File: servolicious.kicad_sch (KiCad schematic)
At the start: 14 parts, among them J1 Conn_01x03_Pin, J10 Barrel_Jack_MountingPin, J2 Conn_01x03_Pin, J3 Conn_01x03_Pin, J4 Conn_01x03_Pin, J5 Conn_01x03_Pin, J6 Conn_01x03_Pin, J7 Conn_01x03_Pin, J8 Conn_01x03_Pin, J9 Conn_01x03_Pin, U2 74HC164

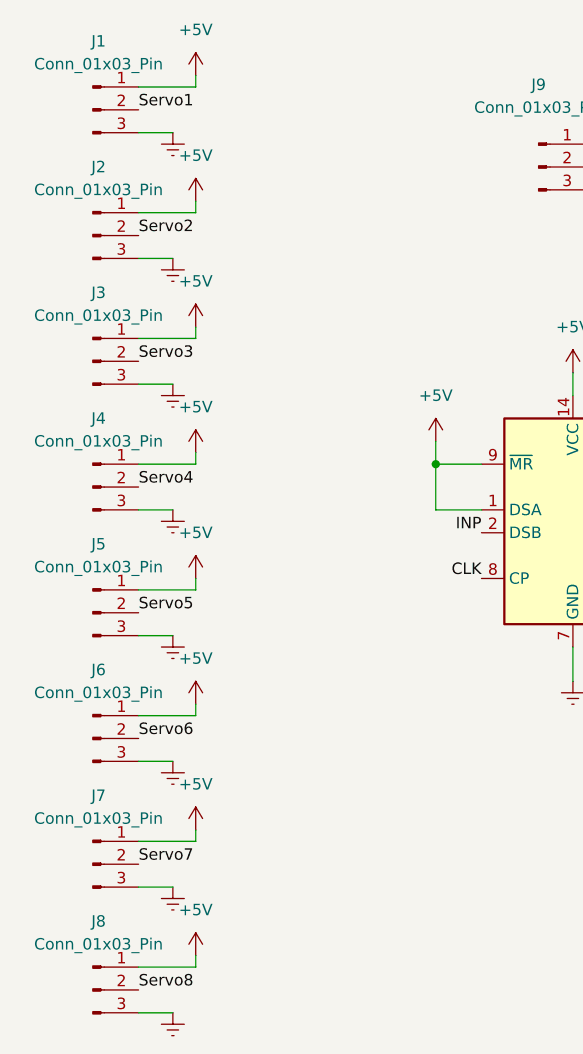
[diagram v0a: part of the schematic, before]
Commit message: Servo headers were wrong
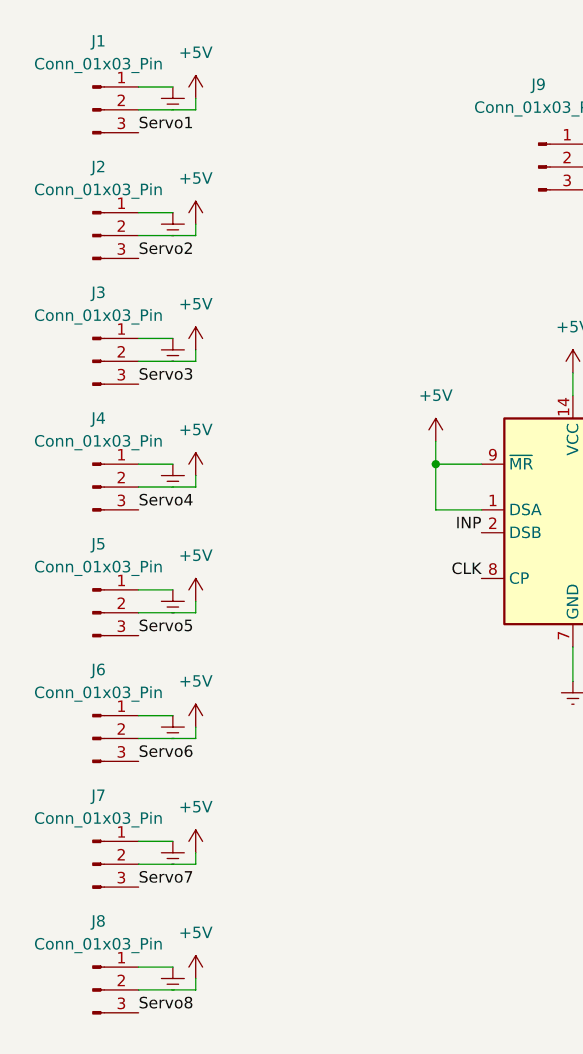
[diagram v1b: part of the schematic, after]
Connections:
- net +5V: now also J1.2 (Pin_2), J2.2 (Pin_2), J3.2 (Pin_2), J4.2 (Pin_2), J5.2 (Pin_2), J6.2 (Pin_2), J7.2 (Pin_2), J8.2 (Pin_2); no longer J1.1 (Pin_1), J2.1 (Pin_1), J3.1 (Pin_1), J4.1 (Pin_1), J5.1 (Pin_1), J6.1 (Pin_1), J7.1 (Pin_1), J8.1 (Pin_1)
- net Earth: now also J1.1 (Pin_1), J2.1 (Pin_1), J3.1 (Pin_1), J4.1 (Pin_1), J5.1 (Pin_1), J6.1 (Pin_1), J7.1 (Pin_1), J8.1 (Pin_1); no longer J1.3 (Pin_3), J2.3 (Pin_3), J3.3 (Pin_3), J4.3 (Pin_3), J5.3 (Pin_3), J6.3 (Pin_3), J7.3 (Pin_3), J8.3 (Pin_3)
- net Servo1: now also J1.3 (Pin_3); no longer J1.2 (Pin_2)
- net Servo2: now also J2.3 (Pin_3); no longer J2.2 (Pin_2)
- net Servo3: now also J3.3 (Pin_3); no longer J3.2 (Pin_2)
- net Servo4: now also J4.3 (Pin_3); no longer J4.2 (Pin_2)
- net Servo5: now also J5.3 (Pin_3); no longer J5.2 (Pin_2)
- net Servo6: now also J6.3 (Pin_3); no longer J6.2 (Pin_2)
- net Servo7: now also J7.3 (Pin_3); no longer J7.2 (Pin_2)
- net Servo8: now also J8.3 (Pin_3); no longer J8.2 (Pin_2)

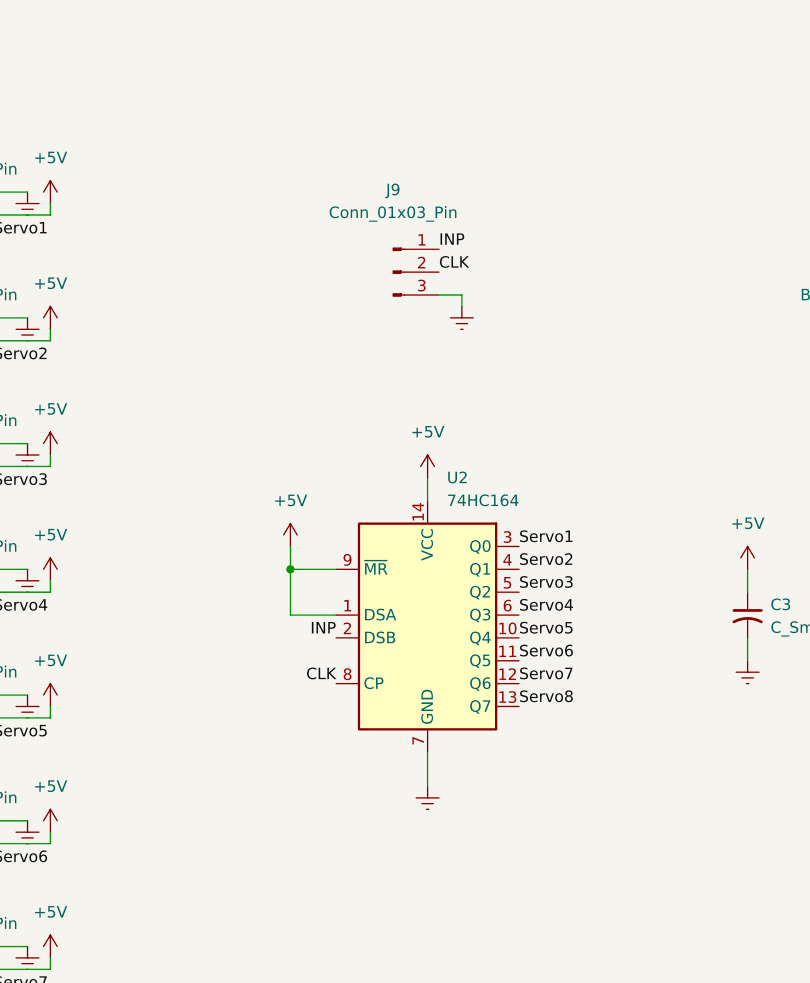
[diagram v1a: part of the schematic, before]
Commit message: Switch to latched shift register
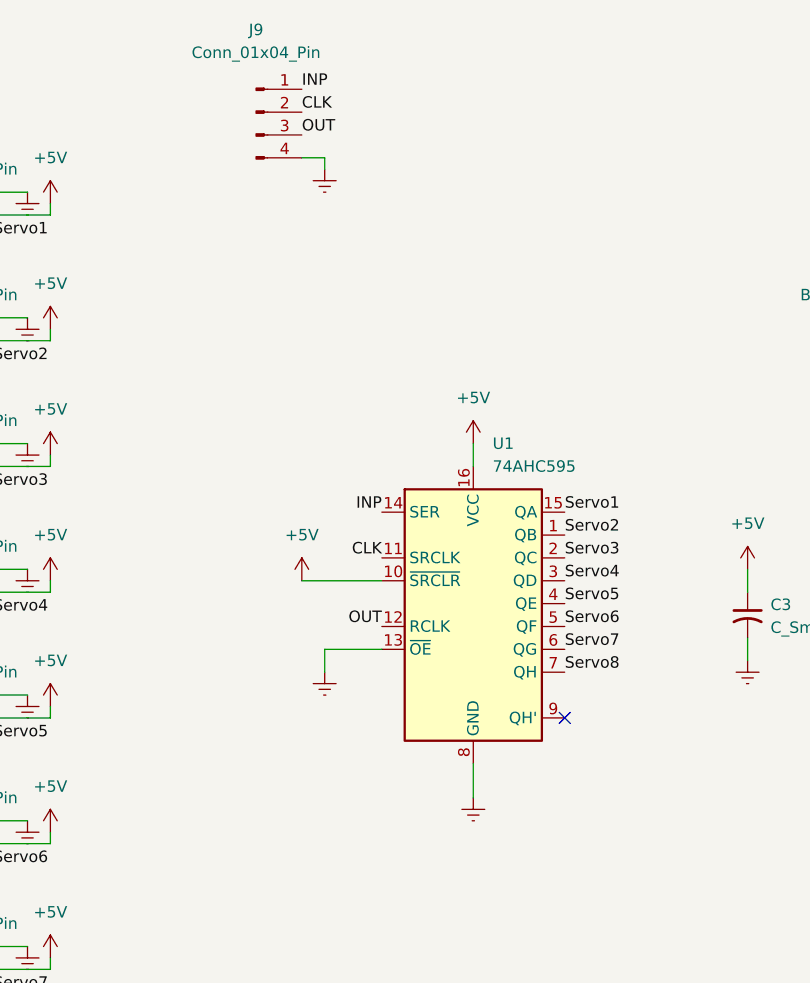
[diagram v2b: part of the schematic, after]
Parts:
- removed J9: Conn_01x03_Pin, Connector_PinHeader_2.54mm:PinHeader_1x03_P2.54mm_Vertical, symbol Connector:Conn_01x03_Pin
- removed U2: 74HC164, Package_SO:SOIC-14_3.9x8.7mm_P1.27mm, symbol 74xx:74HC164
- added J9: Conn_01x04_Pin, Connector_PinHeader_2.54mm:PinHeader_1x04_P2.54mm_Vertical, symbol Connector:Conn_01x04_Pin
- added U1: 74AHC595, Package_SO:SOIC-16W_5.3x10.2mm_P1.27mm, symbol 74xx:74AHC595
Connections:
- net +5V: now also U1.10 (~{SRCLR}), U1.16 (VCC)
- net CLK: now also J9.2 (Pin_2), U1.11 (SRCLK)
- net Earth: now also J9.4 (Pin_4), U1.13 (~{OE}), U1.8 (GND)
- net INP: now also J9.1 (Pin_1), U1.14 (SER)
- net Servo1: now also U1.15 (QA)
- net Servo2: now also U1.1 (QB)
- net Servo3: now also U1.2 (QC)
- net Servo4: now also U1.3 (QD)
- net Servo5: now also U1.4 (QE)
- net Servo6: now also U1.5 (QF)
- net Servo7: now also U1.6 (QG)
- net Servo8: now also U1.7 (QH)
- new net OUT: J9.3 (Pin_3), U1.12 (RCLK)
- no-connect marks 1 -> 2

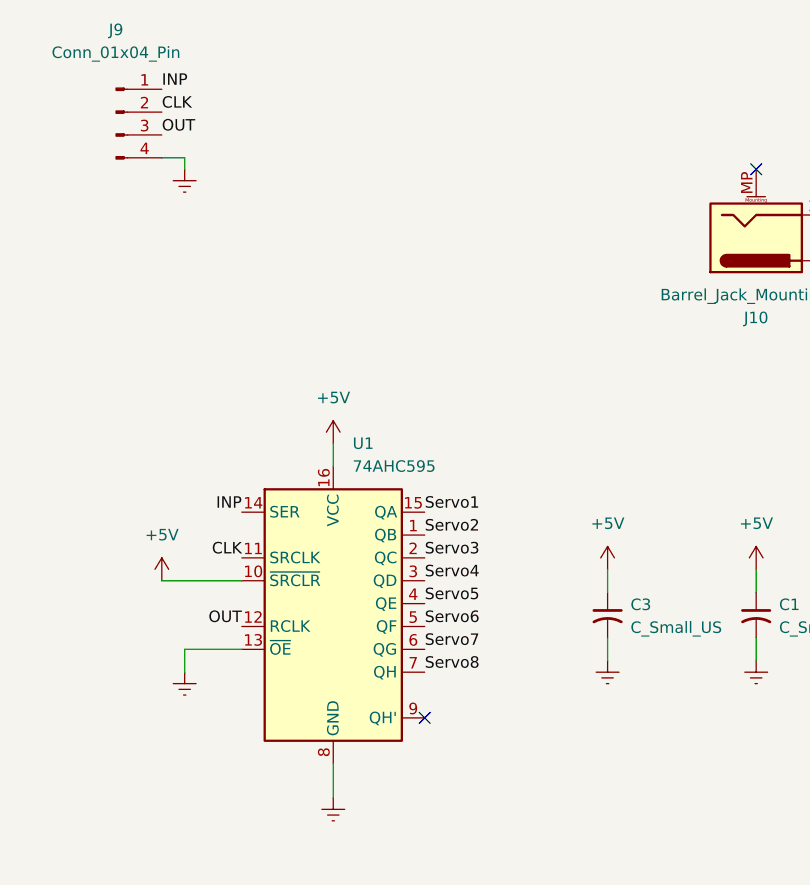
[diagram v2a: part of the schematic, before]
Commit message: Add daisy out
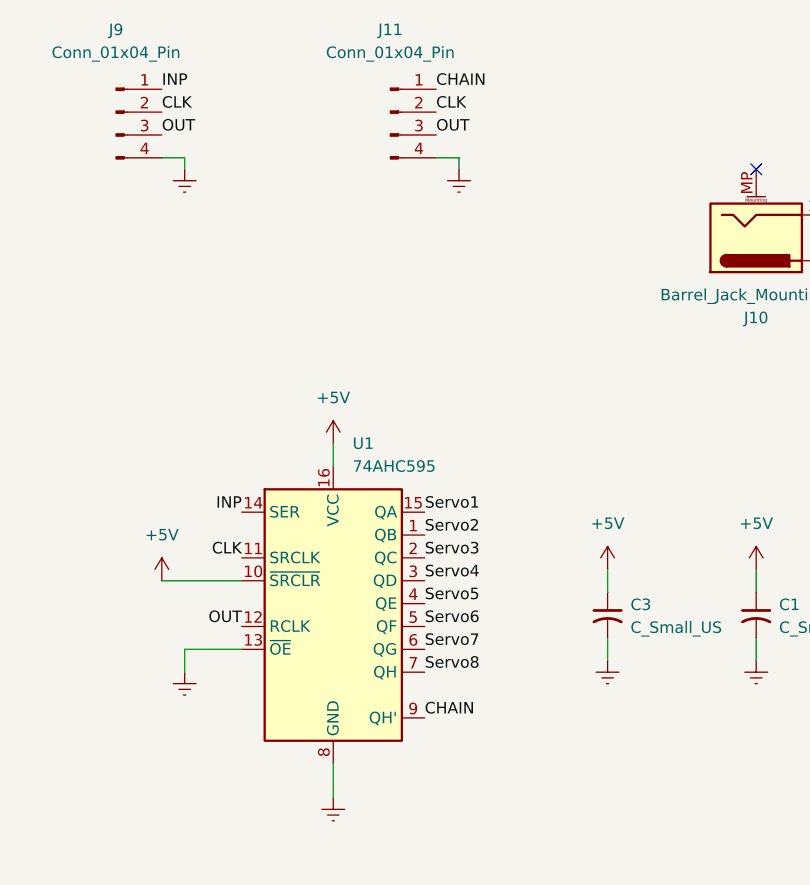
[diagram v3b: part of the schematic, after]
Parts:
- added J11: Conn_01x04_Pin, Connector_PinHeader_2.54mm:PinHeader_1x04_P2.54mm_Vertical, symbol Connector:Conn_01x04_Pin
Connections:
- net CLK: now also J11.2 (Pin_2)
- net Earth: now also J11.4 (Pin_4)
- net OUT: now also J11.3 (Pin_3)
- net CHAIN: now reaches U1.9 (QH')
- net CHAIN: now also J11.1 (Pin_1)
- no-connect marks 2 -> 1
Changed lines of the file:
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@@
 		(at 160.02 46.99)
 	)
-	(no_connect
-		(at 123.19 107.95)
-	)
 	(wire
 		(pts
@@
 	(wire
 		(pts
+			(xy 127 46.99) (xy 127 45.72)
+		)
+		(stroke
+			(width 0)
+			(type default)
+		)
+	)
+	(wire
+		(pts
 			(xy 66.04 66.04) (xy 66.04 64.77)
 		)
@@
 	(wire
 		(pts
+			(xy 127 45.72) (xy 124.46 45.72)
+		)
+		(stroke
+			(width 0)
+			(type default)
+		)
+	)
+	(wire
+		(pts
 			(xy 59.69 66.04) (xy 66.04 66.04)
 		)
@@
 			(width 0)
 			(type default)
+		)
+	)
+	(label "CHAIN"
+		(at 124.46 38.1 0)
+		(effects
+			(font
+				(size 1.27 1.27)
+			)
+			(justify left bottom)
 		)
 	)
@@
 		)
 	)
+	(label "CHAIN"
+		(at 123.19 107.95 0)
+		(effects
+			(font
+				(size 1.27 1.27)
+			)
+			(justify left bottom)
+		)
+	)
 	(label "Servo2"
 		(at 59.69 68.58 0)
@@
 		)
 	)
+	(label "CLK"
+		(at 124.46 40.64 0)
+		(effects
+			(font
+				(size 1.27 1.27)
+			)
+			(justify left bottom)
+		)
+	)
 	(label "OUT"
 		(at 102.87 97.79 180)
@@
 	(label "Servo1"
 		(at 59.69 54.61 0)
+		(effects
+			(font
+				(size 1.27 1.27)
+			)
+			(justify left bottom)
+		)
+	)
+	(label "OUT"
+		(at 124.46 43.18 0)
 		(effects
 			(font
@@
 	(symbol
 		(lib_id "power:Earth")
+		(at 127 46.99 0)
+		(unit 1)
+		(exclude_from_sim no)
+		(in_bom yes)
+		(on_board yes)
+		(dnp no)
+		(fields_autoplaced yes)
+		(property "Reference" "#PWR030"
+			(at 127 53.34 0)
+			(effects
+				(font
+					(size 1.27 1.27)
+				)
+				(hide yes)
+			)
+		)
+		(property "Value" "Earth"
+			(at 127 52.07 0)
+			(effects
+				(font
+					(size 1.27 1.27)
+				)
+				(hide yes)
+			)
+		)
+		(property "Footprint" ""
+			(at 127 46.99 0)
+			(effects
+				(font
+					(size 1.27 1.27)
+				)
+				(hide yes)
+			)
+		)
+		(property "Datasheet" "~"
+			(at 127 46.99 0)
+			(effects
+				(font
+					(size 1.27 1.27)
+				)
+				(hide yes)
+			)
+		)
+		(property "Description" "Power symbol creates a global label with name \"Earth\""
+			(at 127 46.99 0)
+			(effects
+				(font
+					(size 1.27 1.27)
+				)
+				(hide yes)
+			)
+		)
+		(pin "1"
+		)
+		(instances
+			(project "servolicious"
+				(path "/c3a088af-77fe-4a0a-8cb5-e069078caf1a"
+					(reference "#PWR030")
+					(unit 1)
+				)
+			)
+		)
+	)
+	(symbol
+		(lib_id "power:Earth")
 		(at 173.99 60.96 0)
 		(unit 1)
@@
 					(unit 1)
 				)
+			)
+		)
+	)
+	(symbol
+		(lib_id "Connector:Conn_01x04_Pin")
+		(at 119.38 40.64 0)
+		(unit 1)
+		(exclude_from_sim no)
+		(in_bom yes)
+		(on_board yes)
+		(dnp no)
+		(property "Reference" "J11"
+			(at 119.38 31.496 0)
+			(effects
+				(font
+					(size 1.27 1.27)
+				)
+			)
+		)
+		(property "Value" "Conn_01x04_Pin"
+			(at 119.38 34.036 0)
+			(effects
+				(font
+					(size 1.27 1.27)
+				)
+			)
+		)
+		(property "Footprint" "Connector_PinHeader_2.54mm:PinHeader_1x04_P2.54mm_Vertical"
+			(at 119.38 40.64 0)
+			(effects
+				(font
+					(size 1.27 1.27)
+				)
+				(hide yes)
+			)
+		)
+		(property "Datasheet" "~"
+			(at 119.38 40.64 0)
+			(effects
+				(font
+					(size 1.27 1.27)
+				)
+				(hide yes)
+			)
+		)
+		(property "Description" "Generic connector, single row, 01x04, script generated"
+			(at 119.38 40.64 0)
+			(effects
+				(font
+					(size 1.27 1.27)
+				)
+				(hide yes)
+			)
+		)
+		(pin "2"
+		)
+		(pin "4"
+		)
+		(pin "3"
+		)
+		(pin "1"
+		)
+		(instances
+			(project "servolicious"
+				(path "/c3a088af-77fe-4a0a-8cb5-e069078caf1a"
+					(reference "J11")
+					(unit 1)
+				)

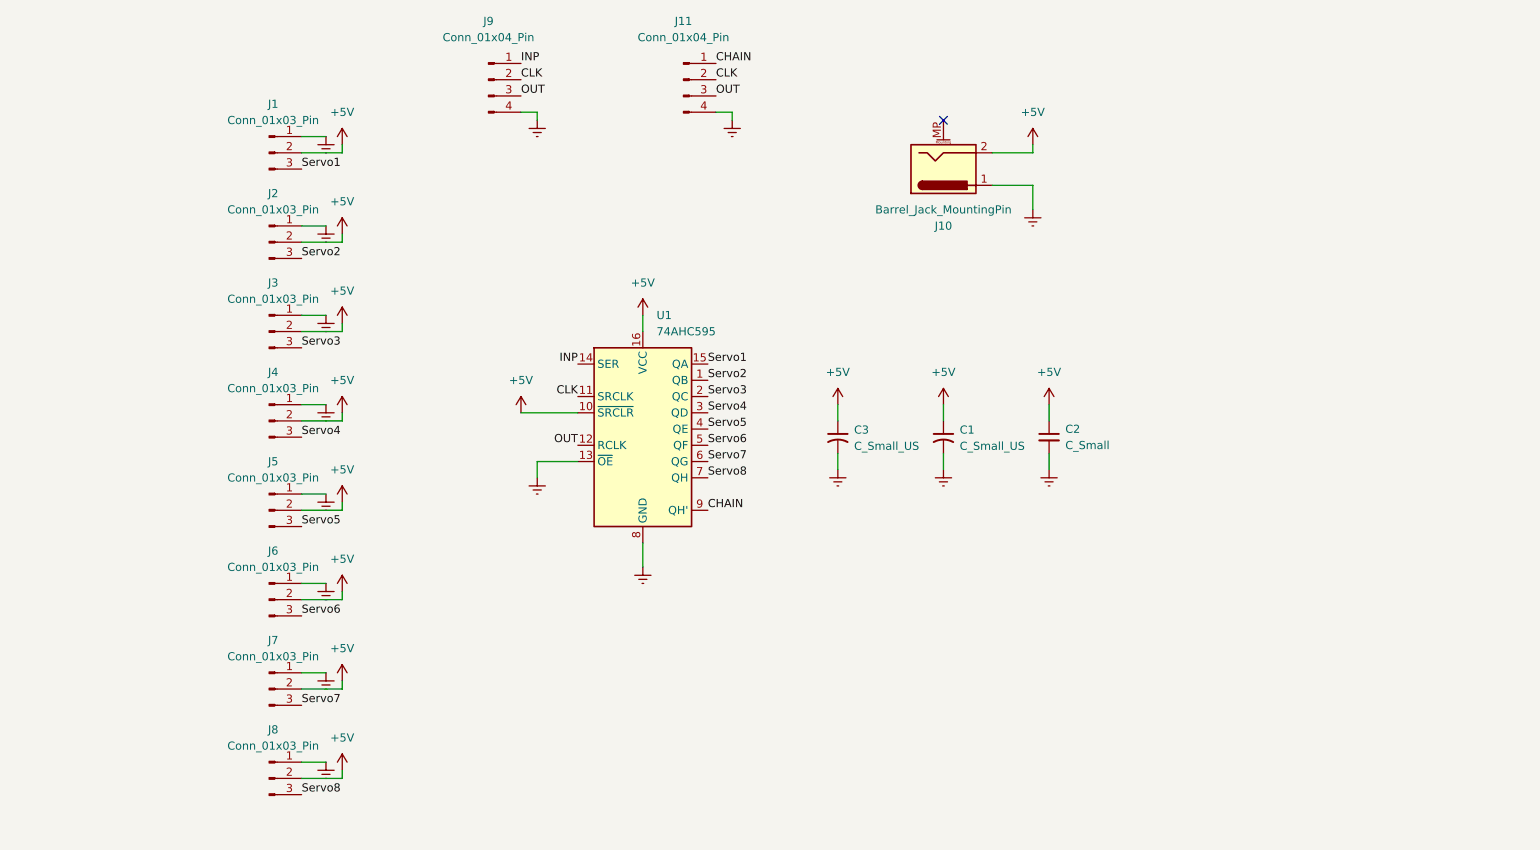
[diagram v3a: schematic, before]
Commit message: Use the PCA9685
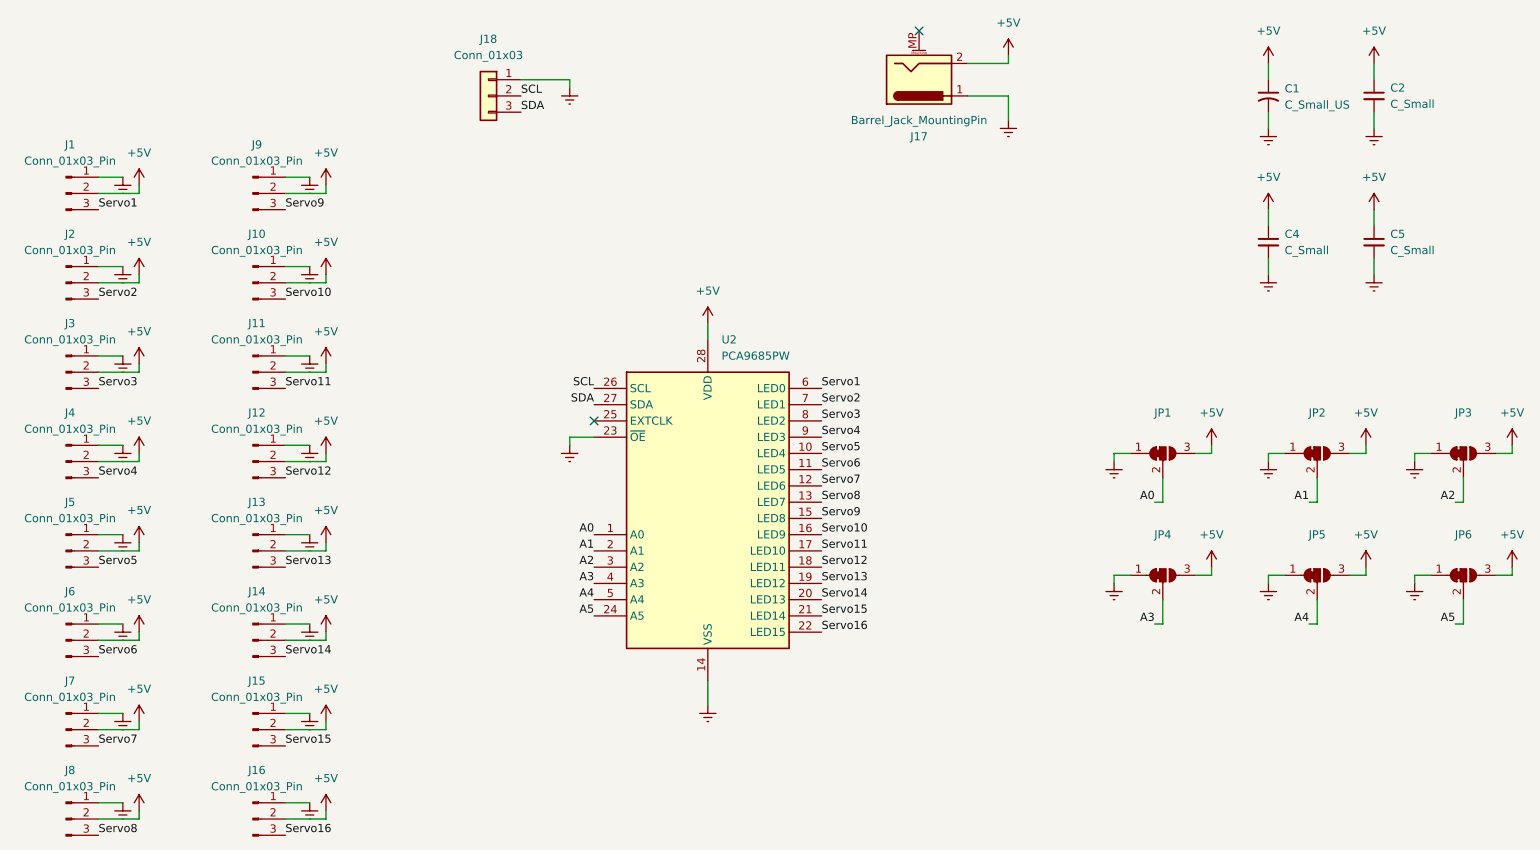
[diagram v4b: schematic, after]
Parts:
- removed C3: C_Small_US, Capacitor_THT:C_Radial_D8.0mm_H11.5mm_P3.50mm, symbol Device:C_Small_US
- removed J11, J9: Conn_01x04_Pin, Connector_PinHeader_2.54mm:PinHeader_1x04_P2.54mm_Vertical, symbol Connector:Conn_01x04_Pin
- removed U1: 74AHC595, Package_SO:SOIC-16W_5.3x10.2mm_P1.27mm, symbol 74xx:74AHC595
- added C4, C5: C_Small, Capacitor_SMD:C_1206_3216Metric_Pad1.33x1.80mm_HandSolder, symbol Device:C_Small
- added J10, J11, J12, J13, J14, J15, J16, J9: Conn_01x03_Pin, Connector_PinHeader_2.54mm:PinHeader_1x03_P2.54mm_Vertical, symbol Connector:Conn_01x03_Pin
- added J18: Conn_01x03, Connector_PinSocket_2.54mm:PinSocket_1x03_P2.54mm_Vertical, symbol Connector_Generic:Conn_01x03
- added JP1, JP2, JP3, JP4, JP5, JP6: Jumper:SolderJumper-3_P1.3mm_Bridged12_RoundedPad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, Jumper:SolderJumper-3_P1.3mm_Bridged12_RoundedPad1.0x1.5mm, symbol Jumper:SolderJumper_3_Bridged12
- added U2: PCA9685PW, Package_SO:TSSOP-28_4.4x9.7mm_P0.65mm, symbol Driver_LED:PCA9685PW
- renumbered J10 to J17
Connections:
- net +5V: now also C4.1, C5.1, J10.2 (Pin_2), J11.2 (Pin_2), J12.2 (Pin_2), J13.2 (Pin_2), J14.2 (Pin_2), J15.2 (Pin_2), J16.2 (Pin_2), J9.2 (Pin_2), JP1.3 (B), JP2.3 (B), JP3.3 (B), JP4.3 (B), JP5.3 (B), JP6.3 (B), U2.28 (VDD)
- net Earth: now also C4.2, C5.2, J10.1 (Pin_1), J11.1 (Pin_1), J12.1 (Pin_1), J13.1 (Pin_1), J14.1 (Pin_1), J15.1 (Pin_1), J16.1 (Pin_1), J18.1 (Pin_1), J9.1 (Pin_1), JP1.1 (A), JP2.1 (A), JP3.1 (A), JP4.1 (A), JP5.1 (A), JP6.1 (A), U2.14 (VSS), U2.23 (~{OE})
- net Servo1: now also U2.6 (LED0)
- net Servo2: now also U2.7 (LED1)
- net Servo3: now also U2.8 (LED2)
- net Servo4: now also U2.9 (LED3)
- net Servo5: now also U2.10 (LED4)
- net Servo6: now also U2.11 (LED5)
- net Servo7: now also U2.12 (LED6)
- net Servo8: now also U2.13 (LED7)
- new net A0: JP1.2 (C), U2.1 (A0)
- new net A1: JP2.2 (C), U2.2 (A1)
- new net A2: JP3.2 (C), U2.3 (A2)
- new net A3: JP4.2 (C), U2.4 (A3)
- new net A4: JP5.2 (C), U2.5 (A4)
- new net A5: JP6.2 (C), U2.24 (A5)
- new net SCL: J18.2 (Pin_2), U2.26 (SCL)
- new net SDA: J18.3 (Pin_3), U2.27 (SDA)
- new net Servo10: J10.3 (Pin_3), U2.16 (LED9)
- new net Servo11: J11.3 (Pin_3), U2.17 (LED10)
- new net Servo12: J12.3 (Pin_3), U2.18 (LED11)
- new net Servo13: J13.3 (Pin_3), U2.19 (LED12)
- new net Servo14: J14.3 (Pin_3), U2.20 (LED13)
- new net Servo15: J15.3 (Pin_3), U2.21 (LED14)
- new net Servo16: J16.3 (Pin_3), U2.22 (LED15)
- new net Servo9: J9.3 (Pin_3), U2.15 (LED8)
- no-connect marks 1 -> 2
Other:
- moved on the sheet: C1, C2, J1, J17, J2, J3, J4, J5, J6, J7, J8
